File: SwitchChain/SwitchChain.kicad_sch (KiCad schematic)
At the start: 1 part, among them J101 Conn_01x06

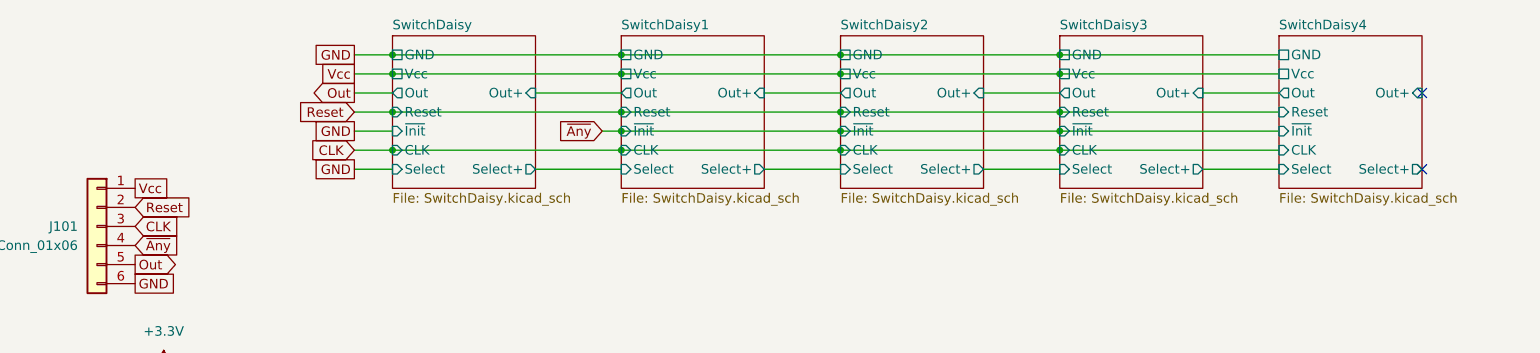
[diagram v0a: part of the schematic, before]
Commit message: fix pin label, reduce column keys to 4
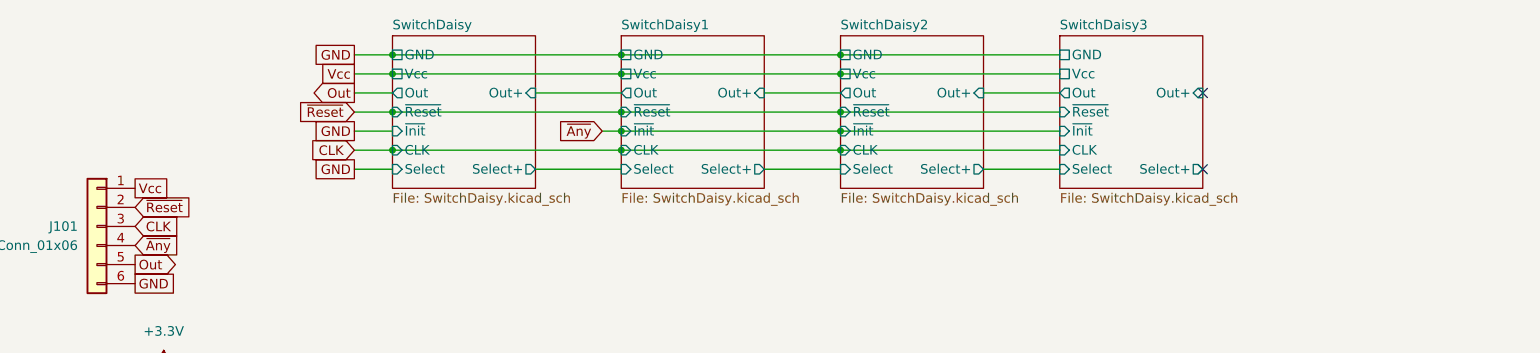
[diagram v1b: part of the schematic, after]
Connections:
- net Reset renamed ~{Reset}
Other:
- removed sheet SwitchDaisy4
- sheet SwitchDaisy ports: added ~{Reset}; removed Reset
- sheet SwitchDaisy1 ports: added ~{Reset}; removed Reset
- sheet SwitchDaisy2 ports: added ~{Reset}; removed Reset
- sheet SwitchDaisy3 ports: added ~{Reset}; removed Reset

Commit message: fix circuit
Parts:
- added U101: 74HC00, Package_DFN_QFN:WQFN-14-1EP_2.5x2.5mm_P0.5mm_EP1.45x1.45mm, symbol 74xx:74HC00
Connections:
- net +3.3V: now also U101.14 (VCC)
- net GND: now also U101.1, U101.2, U101.4, U101.5, U101.7 (GND)
- net ~{Any}: now also U101.10
- net ~{Reset}: now also U101.9
- new net: U101.12, U101.13, U101.8
- new net SwitchDaisy/~{Init}: U101.11
- no-connect marks 2 -> 4

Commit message: change connector
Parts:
- J101: Manufacturer Part number (none) -> 2005280060; Original (none) -> N; Purchase Link (none) -> https://www.digikey.com/en/products/detail/molex/2005280060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
- U101: Manufacturer Part number (none) -> SN74HCS00BQAR; Original (none) -> N; Purchase Link (none) -> https://www.digikey.com/en/products/detail/texas-instrument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
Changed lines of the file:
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@@
+			)
+		)
+		(property "Manufacturer Part number" "SN74HCS00BQAR"
+			(at 157.48 106.68 0)
+			(effects
+				(font
+					(size 1.27 1.27)
+				)
+				(hide yes)
+			)
+		)
+		(property "Original" "N"
+			(at 157.48 106.68 0)
+			(effects
+				(font
+					(size 1.27 1.27)
+				)
+				(hide yes)
+			)
+		)
+		(property "Purchase Link" "https://www.digikey.com/en/products/detail/texas-instruments/SN74HCS00BQAR/13896419"
+			(at 157.48 106.68 0)
+			(effects
+				(font
+					(size 1.27 1.27)
+				)
+				(hide yes)
 			)
 		)
@@
 			)
 		)
+		(property "Manufacturer Part number" "SN74HCS00BQAR"
+			(at 157.48 118.11 0)
+			(effects
+				(font
+					(size 1.27 1.27)
+				)
+				(hide yes)
+			)
+		)
+		(property "Original" "N"
+			(at 157.48 118.11 0)
+			(effects
+				(font
+					(size 1.27 1.27)
+				)
+				(hide yes)
+			)
+		)
+		(property "Purchase Link" "https://www.digikey.com/en/products/detail/texas-instruments/SN74HCS00BQAR/13896419"
+			(at 157.48 118.11 0)
+			(effects
+				(font
+					(size 1.27 1.27)
+				)
+				(hide yes)
+			)
+		)
 		(pin "1"
 		)
@@
 			)
 		)
+		(property "Manufacturer Part number" "SN74HCS00BQAR"
+			(at 105.41 78.74 0)
+			(effects
+				(font
+					(size 1.27 1.27)
+				)
+				(hide yes)
+			)
+		)
+		(property "Original" "N"
+			(at 105.41 78.74 0)
+			(effects
+				(font
+					(size 1.27 1.27)
+				)
+				(hide yes)
+			)
+		)
+		(property "Purchase Link" "https://www.digikey.com/en/products/detail/texas-instruments/SN74HCS00BQAR/13896419"
+			(at 105.41 78.74 0)
+			(effects
+				(font
+					(size 1.27 1.27)
+				)
+				(hide yes)
+			)
+		)
 		(pin "1"
 		)
@@
 			)
 		)
+		(property "Manufacturer Part number" "SN74HCS00BQAR"
+			(at 133.35 110.49 0)
+			(effects
+				(font
+					(size 1.27 1.27)
+				)
+				(hide yes)
+			)
+		)
+		(property "Original" "N"
+			(at 133.35 110.49 0)
+			(effects
+				(font
+					(size 1.27 1.27)
+				)
+				(hide yes)
+			)
+		)
+		(property "Purchase Link" "https://www.digikey.com/en/products/detail/texas-instruments/SN74HCS00BQAR/13896419"
+			(at 133.35 110.49 0)
+			(effects
+				(font
+					(size 1.27 1.27)
+				)
+				(hide yes)
+			)
+		)
 		(pin "1"
 		)
@@
 			)
 		)
-		(property "Description" "Generic connector, single row, 01x06, script generated (kicad-library-utils/schlib/autogen/connector/)"
+		(property "Description" "CONN FFC FPC BOTTOM 6POS 1MM R/A"
+			(at 82.55 91.44 0)
+			(effects
+				(font
+					(size 1.27 1.27)
+				)
+				(hide yes)
+			)
+		)
+		(property "Manufacturer Part number" "2005280060"
+			(at 82.55 91.44 0)
+			(effects
+				(font
+					(size 1.27 1.27)
+				)
+				(hide yes)
+			)
+		)
+		(property "Original" "N"
+			(at 82.55 91.44 0)
+			(effects
+				(font
+					(size 1.27 1.27)
+				)
+				(hide yes)
+			)
+		)
+		(property "Purchase Link" "https://www.digikey.com/en/products/detail/molex/2005280060/6099556"
 			(at 82.55 91.44 0)
 			(effects
@@
 			(at 88.9 78.74 0)
 			(effects
+				(font
+					(size 1.27 1.27)
+				)
+				(hide yes)
+			)
+		)
+		(property "Manufacturer Part number" "SN74HCS00BQAR"
+			(at 88.9 78.74 0)
+			(effects
+				(font
+					(size 1.27 1.27)
+				)
+				(hide yes)
+			)
+		)
+		(property "Original" "N"
+			(at 88.9 78.74 0)
+			(effects
+				(font
+					(size 1.27 1.27)
+				)
+				(hide yes)
+			)
+		)
+		(property "Purchase Link" "https://www.digikey.com/en/products/detail/texas-instruments/SN74HCS00BQAR/13896419"
+			(at 88.9 78.74 0)
+			(effects

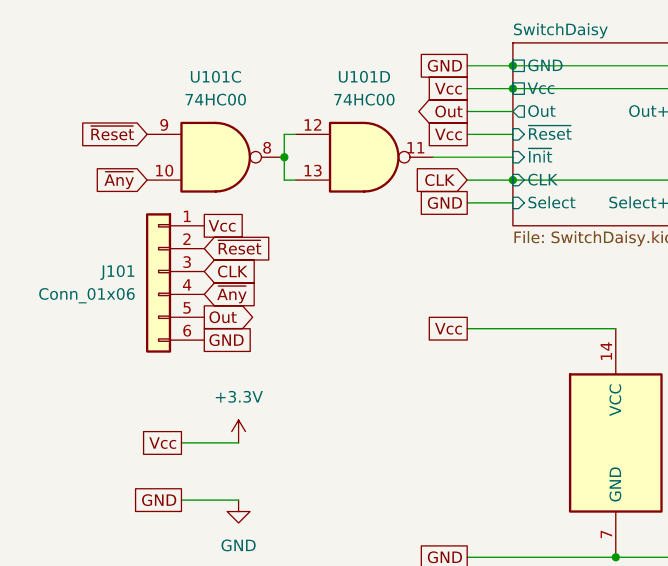
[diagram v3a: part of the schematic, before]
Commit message: flip connector
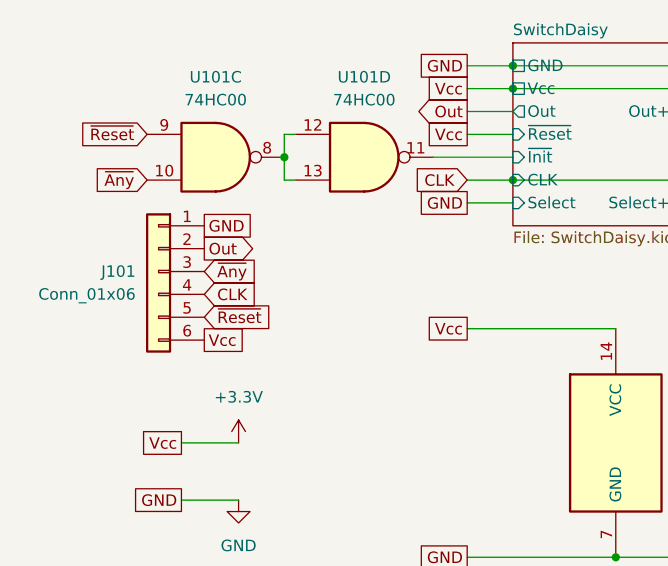
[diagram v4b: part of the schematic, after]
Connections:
- net +3.3V: now also J101.6 (Pin_6); no longer J101.1 (Pin_1)
- net CLK: now also J101.4 (Pin_4); no longer J101.3 (Pin_3)
- net GND: now also J101.1 (Pin_1); no longer J101.6 (Pin_6)
- net Out: now also J101.2 (Pin_2); no longer J101.5 (Pin_5)
- net ~{Any}: now also J101.3 (Pin_3); no longer J101.4 (Pin_4)
- net ~{Reset}: now also J101.5 (Pin_5); no longer J101.2 (Pin_2)
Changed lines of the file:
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@@
 	(global_label "~{Reset}"
 		(shape input)
-		(at 87.63 88.9 0)
-		(fields_autoplaced yes)
-		(effects
-			(font
-				(size 1.27 1.27)
-			)
-			(justify left)
-		)
-		(property "Intersheetrefs" "${INTERSHEET_REFS}"
-			(at 95.8162 88.9 0)
+		(at 87.63 96.52 0)
+		(fields_autoplaced yes)
+		(effects
+			(font
+				(size 1.27 1.27)
+			)
+			(justify left)
+		)
+		(property "Intersheetrefs" "${INTERSHEET_REFS}"
+			(at 95.8162 96.52 0)
 			(effects
 				(font
@@
 	(global_label "Out"
 		(shape output)
-		(at 87.63 96.52 0)
-		(fields_autoplaced yes)
-		(effects
-			(font
-				(size 1.27 1.27)
-			)
-			(justify left)
-		)
-		(property "Intersheetrefs" "${INTERSHEET_REFS}"
-			(at 93.8204 96.52 0)
+		(at 87.63 88.9 0)
+		(fields_autoplaced yes)
+		(effects
+			(font
+				(size 1.27 1.27)
+			)
+			(justify left)
+		)
+		(property "Intersheetrefs" "${INTERSHEET_REFS}"
+			(at 93.8204 88.9 0)
 			(effects
 				(font
@@
 	(global_label "~{Any}"
 		(shape input)
+		(at 87.63 91.44 0)
+		(fields_autoplaced yes)
+		(effects
+			(font
+				(size 1.27 1.27)
+			)
+			(justify left)
+		)
+		(property "Intersheetrefs" "${INTERSHEET_REFS}"
+			(at 93.8204 91.44 0)
+			(effects
+				(font
+					(size 1.27 1.27)
+				)
+				(justify left)
+				(hide yes)
+			)
+		)
+	)
+	(global_label "~{Reset}"
+		(shape input)
+		(at 81.28 76.2 180)
+		(fields_autoplaced yes)
+		(effects
+			(font
+				(size 1.27 1.27)
+			)
+			(justify right)
+		)
+		(property "Intersheetrefs" "${INTERSHEET_REFS}"
+			(at 73.0938 76.2 0)
+			(effects
+				(font
+					(size 1.27 1.27)
+				)
+				(justify right)
+				(hide yes)
+			)
+		)
+	)
+	(global_label "~{Any}"
+		(shape input)
+		(at 81.28 81.28 180)
+		(fields_autoplaced yes)
+		(effects
+			(font
+				(size 1.27 1.27)
+			)
+			(justify right)
+		)
+		(property "Intersheetrefs" "${INTERSHEET_REFS}"
+			(at 75.0896 81.28 0)
+			(effects
+				(font
+					(size 1.27 1.27)
+				)
+				(justify right)
+				(hide yes)
+			)
+		)
+	)
+	(global_label "CLK"
+		(shape input)
 		(at 87.63 93.98 0)
 		(fields_autoplaced yes)
@@
 		)
 		(property "Intersheetrefs" "${INTERSHEET_REFS}"
-			(at 93.8204 93.98 0)
-			(effects
-				(font
-					(size 1.27 1.27)
-				)
-				(justify left)
+			(at 94.1833 93.98 0)
+			(effects
+				(font
+					(size 1.27 1.27)
+				)
+				(justify left)
+				(hide yes)
+			)
+		)
+	)
+	(global_label "GND"
+		(shape passive)
+		(at 116.84 83.82 180)
+		(fields_autoplaced yes)
+		(effects
+			(font
+				(size 1.27 1.27)
+			)
+			(justify right)
+		)
+		(property "Intersheetrefs" "${INTERSHEET_REFS}"
+			(at 111.0956 83.82 0)
+			(effects
+				(font
+					(size 1.27 1.27)
+				)
+				(justify right)
+				(hide yes)
+			)
+		)
+	)
+	(global_label "Vcc"
+		(shape passive)
+		(at 116.84 97.79 180)
+		(fields_autoplaced yes)
+		(effects
+			(font
+				(size 1.27 1.27)
+			)
+			(justify right)
+		)
+		(property "Intersheetrefs" "${INTERSHEET_REFS}"
+			(at 111.7003 97.79 0)
+			(effects
+				(font
+					(size 1.27 1.27)
+				)
+				(justify right)
 				(hide yes)
 			)
@@
 	(global_label "~{Reset}"
 		(shape input)
-		(at 81.28 76.2 180)
-		(fields_autoplaced yes)
-		(effects
-			(font
-				(size 1.27 1.27)
-			)
-			(justify right)
-		)
-		(property "Intersheetrefs" "${INTERSHEET_REFS}"
-			(at 73.0938 76.2 0)
-			(effects
-				(font
-					(size 1.27 1.27)
-				)
-				(justify right)
-				(hide yes)
-			)
-		)
-	)
-	(global_label "~{Any}"
-		(shape input)
-		(at 81.28 81.28 180)
-		(fields_autoplaced yes)
-		(effects
-			(font
-				(size 1.27 1.27)
-			)
-			(justify right)
-		)
-		(property "Intersheetrefs" "${INTERSHEET_REFS}"
-			(at 75.0896 81.28 0)
-			(effects
-				(font
-					(size 1.27 1.27)
-				)
-				(justify right)
-				(hide yes)
-			)
-		)
-	)
-	(global_label "CLK"
-		(shape input)
-		(at 87.63 91.44 0)
-		(fields_autoplaced yes)
-		(effects
-			(font
-				(size 1.27 1.27)
-			)
-			(justify left)
-		)
-		(property "Intersheetrefs" "${INTERSHEET_REFS}"
-			(at 94.1833 91.44 0)
-			(effects
-				(font
-					(size 1.27 1.27)
-				)
-				(justify left)
-				(hide yes)
-			)
-		)
-	)
-	(global_label "GND"
-		(shape passive)
-		(at 116.84 83.82 180)
-		(fields_autoplaced yes)
-		(effects
-			(font
-				(size 1.27 1.27)
-			)
-			(justify right)
-		)
-		(property "Intersheetrefs" "${INTERSHEET_REFS}"
-			(at 111.0956 83.82 0)
+		(at 149.86 76.2 180)
+		(fields_autoplaced yes)
+		(effects
+			(font
+				(size 1.27 1.27)
+			)
+			(justify right)
+		)
+		(property "Intersheetrefs" "${INTERSHEET_REFS}"
+			(at 141.6738 76.2 0)
 			(effects
 				(font
@@
 	(global_label "Vcc"
 		(shape passive)
-		(at 116.84 97.79 180)
-		(fields_autoplaced yes)
-		(effects
-			(font
-				(size 1.27 1.27)
-			)
-			(justify right)
-		)
-		(property "Intersheetrefs" "${INTERSHEET_REFS}"
-			(at 111.7003 97.79 0)
-			(effects
-				(font
-					(size 1.27 1.27)
-				)
-				(justify right)
-				(hide yes)
-			)
-		)
-	)
-	(global_label "~{Reset}"
-		(shape input)
-		(at 149.86 76.2 180)
-		(fields_autoplaced yes)
-		(effects
-			(font
-				(size 1.27 1.27)
-			)
-			(justify right)
-		)
-		(property "Intersheetrefs" "${INTERSHEET_REFS}"
-			(at 141.6738 76.2 0)
-			(effects
-				(font
-					(size 1.27 1.27)
-				)
-				(justify right)
-				(hide yes)
-			)
-		)
-	)
-	(global_label "Vcc"
-		(shape passive)
-		(at 87.63 86.36 0)
-		(fields_autoplaced yes)
-		(effects
-			(font
-				(size 1.27 1.27)
-			)
-			(justify left)
-		)
-		(property "Intersheetrefs" "${INTERSHEET_REFS}"
-			(at 92.7697 86.36 0)
+		(at 87.63 99.06 0)
+		(fields_autoplaced yes)
+		(effects
+			(font
+				(size 1.27 1.27)
+			)
+			(justify left)
+		)
+		(property "Intersheetrefs" "${INTERSHEET_REFS}"
+			(at 92.7697 99.06 0)
 			(effects
 				(font
@@
 	(global_label "GND"
 		(shape passive)
-		(at 87.63 99.06 0)
-		(fields_autoplaced yes)
-		(effects
-			(font
-				(size 1.27 1.27)
-			)
-			(justify left)
-		)
-		(property "Intersheetrefs" "${INTERSHEET_REFS}"
-			(at 93.3744 99.06 0)
-			(effects
-				(font
+		(at 87.63 86.36 0)
+		(fields_autoplaced yes)
+		(effects
+			(font
+				(size 1.27 1.27)
+			)
+			(justify left)
+		)
+		(property "Intersheetrefs" "${INTERSHEET_REFS}"
+			(at 93.3744 86.36 0)
+			(effects
+				(font
